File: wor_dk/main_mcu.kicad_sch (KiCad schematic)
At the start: 35 parts, among them IC201 TMUX1112PWR, IC202 TMUX1112PWR, J201 Prog_DUT, J202 Conn_02x04_Odd_Even, SW201 SW_Push, U201 nRF52840, Y201 32.768kHz, Y202 32MHz

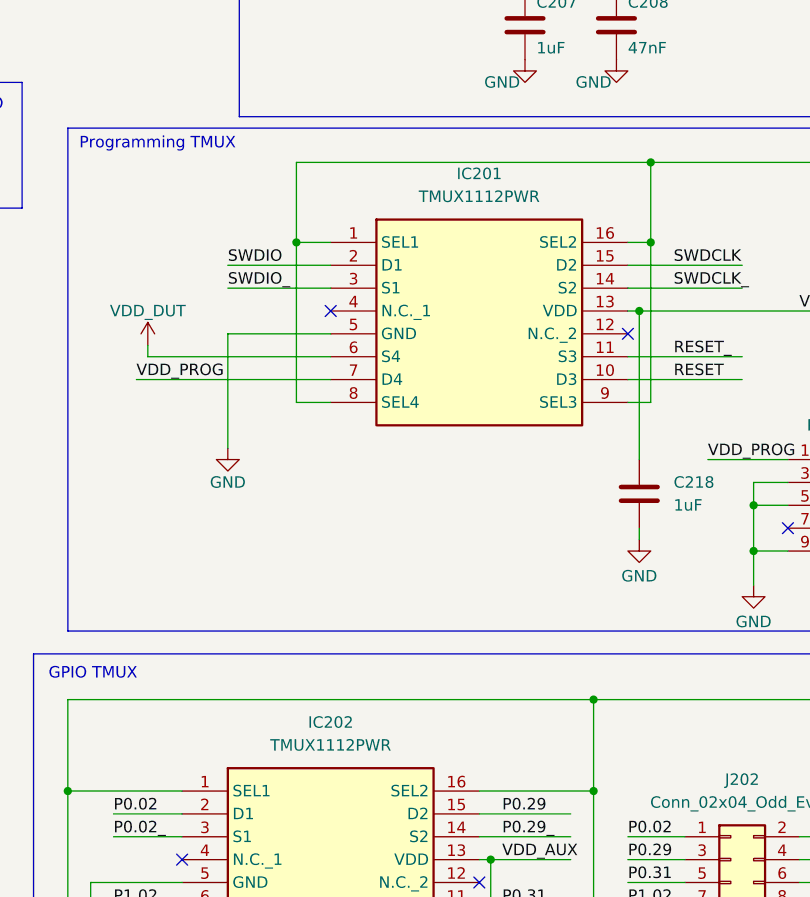
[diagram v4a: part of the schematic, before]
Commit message: wor_dk: library reorganization
- move everything to components
- use same directory naming as KiCAD installation
  (symbols/footprints/3dmodels)
- collect components into libraries rather than adding each file
  individually
- sanitize symbols according to our guidelines
  - sanitize symbol fields (e.g. Manufacturer Part Number -> MPN)
  - sanitize reference (IC -> U)
  - add ImportOrigin
  - add LCSC part number
  - remove unused fields
- link 3D models in footprints
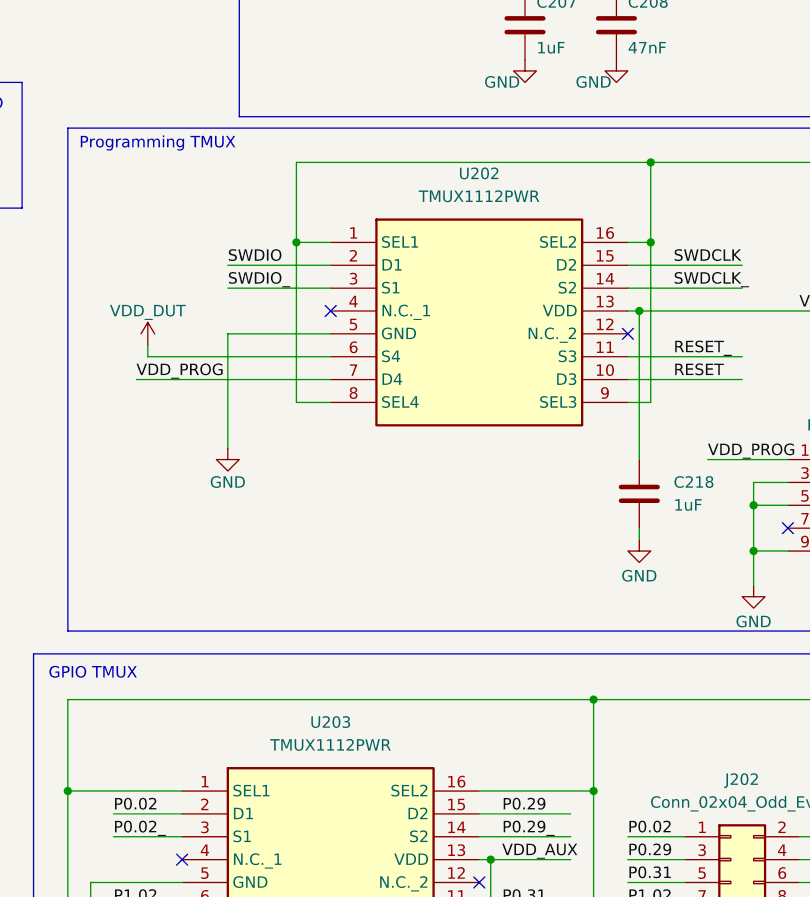
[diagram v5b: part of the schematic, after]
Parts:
- removed IC201, IC202: TMUX1112PWR, SOP65P640X120-16N, symbol TMUX1112PWR:TMUX1112PWR
- added U202, U203: TMUX1112PWR, TexasInstruments:SOP65P640X120-16N, symbol TexasInstruments:TMUX1112PWR
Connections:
- net GND: now also U202.5 (GND), U203.5 (GND)
- net GPIO_EN: now also U203.1 (SEL1), U203.16 (SEL2), U203.8 (SEL4), U203.9 (SEL3)
- net P0.02: now also U203.2 (D1)
- net P0.02_: now also U203.3 (S1)
- net P0.29: now also U203.15 (D2)
- net P0.29_: now also U203.14 (S2)
- net P0.31: now also U203.10 (D3)
- net P0.31_: now also U203.11 (S3)
- net P1.02: now also U203.7 (D4)
- net P1.02_: now also U203.6 (S4)
- net PROG_EN: now also U202.1 (SEL1), U202.16 (SEL2), U202.8 (SEL4), U202.9 (SEL3)
- net RESET: now also U202.10 (D3)
- net RESET_: now also U202.11 (S3)
- net SWDCLK: now also U202.15 (D2)
- net SWDCLK_: now also U202.14 (S2)
- net SWDIO: now also U202.2 (D1)
- net SWDIO_: now also U202.3 (S1)
- net VDD_AUX: now also U202.13 (VDD), U203.13 (VDD)
- net VDD_DUT: now also U202.6 (S4)
- net VDD_PROG: now also U202.7 (D4)

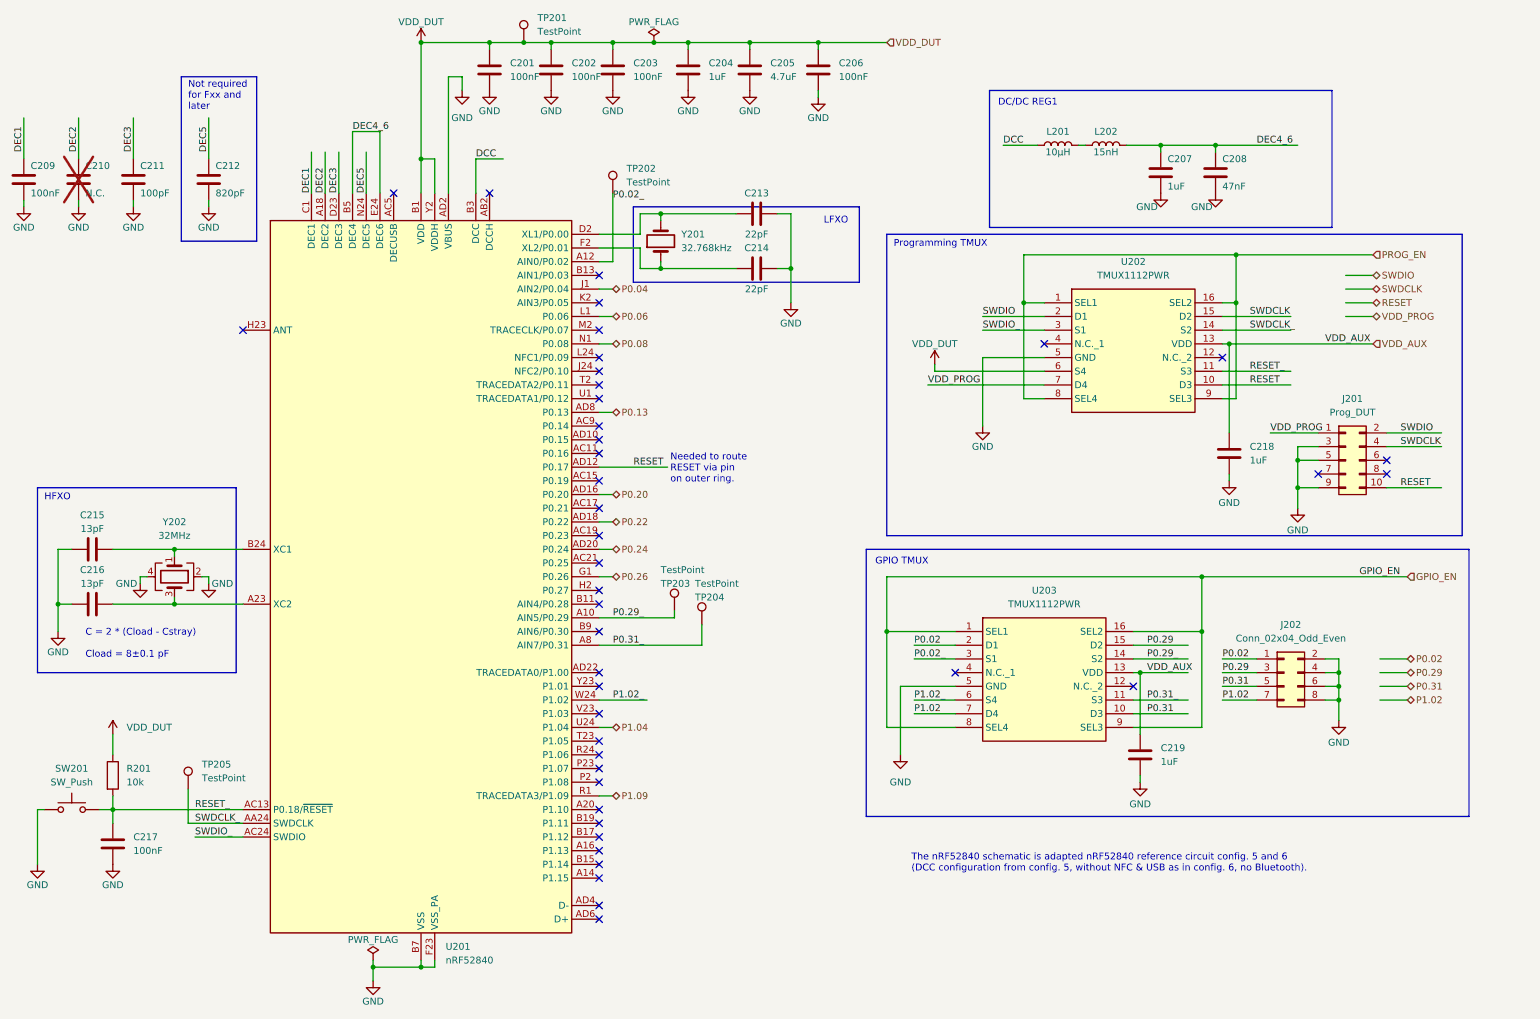
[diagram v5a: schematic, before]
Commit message: wor_dk: top-level connections & cleanup
- top-level connections for TMUX control & UART done (selection
  between FTDI and DAP Link via jumpers)
- all ERC errors & warnings cleaned up
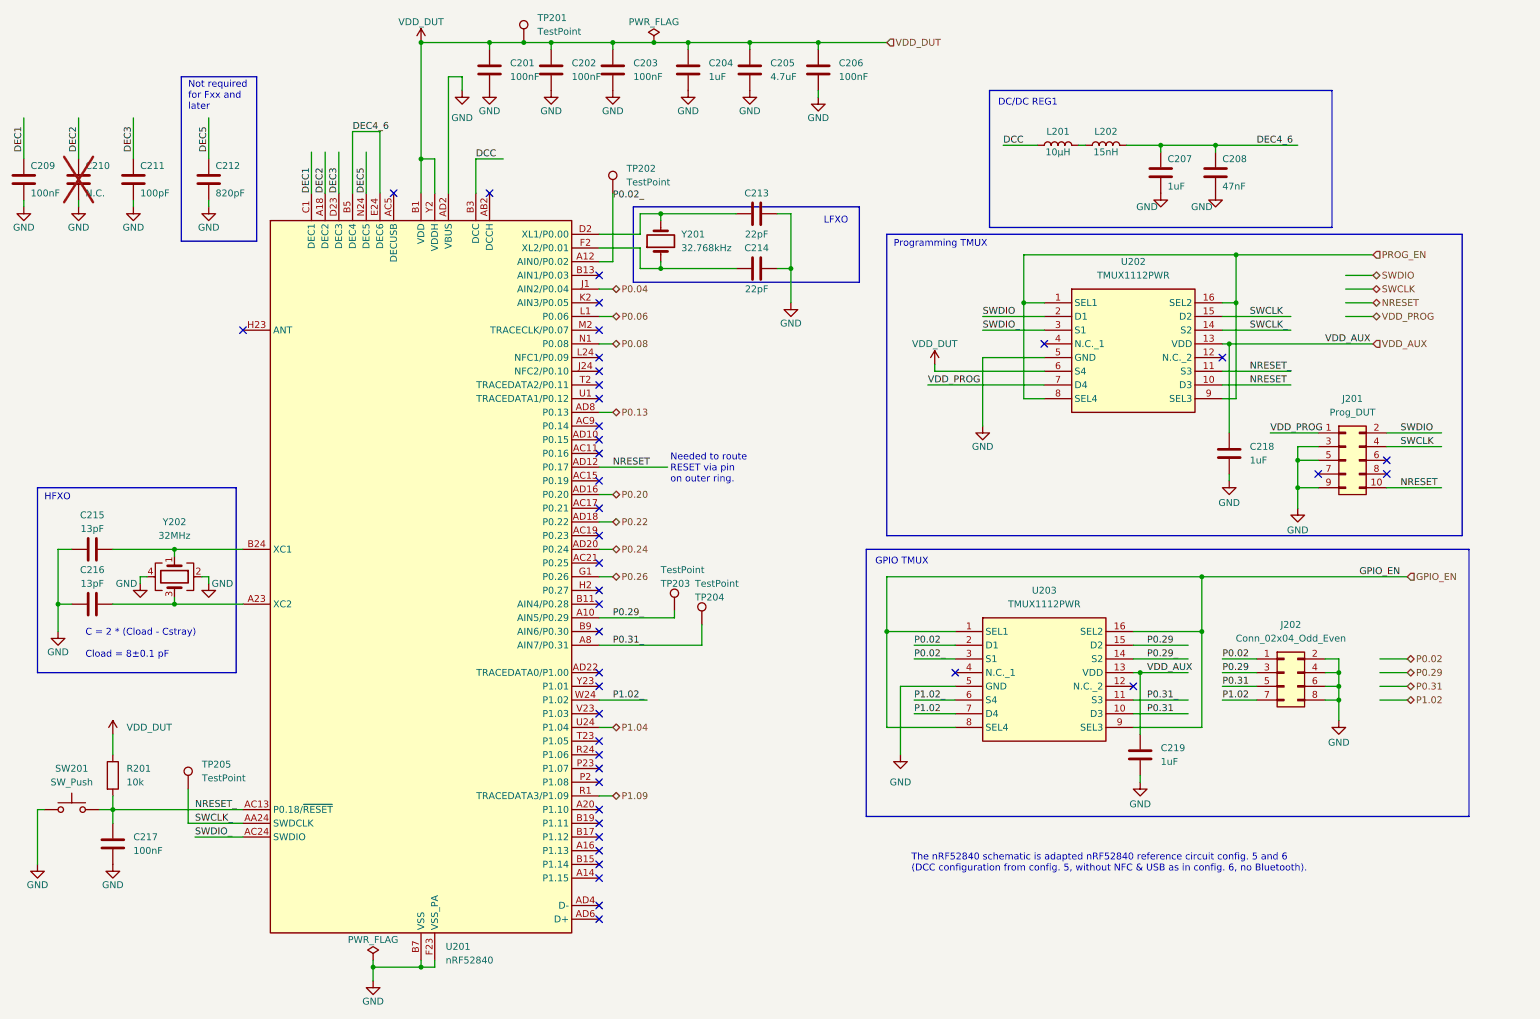
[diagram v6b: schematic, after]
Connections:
- net RESET renamed NRESET
- net RESET_ renamed NRESET_
- net SWDCLK renamed SWCLK
- net SWDCLK_ renamed SWCLK_
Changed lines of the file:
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@@
 		)
 	)
-	(label "SWDCLK"
+	(label "SWCLK"
 		(at 270.51 93.98 0)
 		(fields_autoplaced yes)
@@
 		)
 	)
-	(label "SWDCLK"
+	(label "SWCLK"
 		(at 242.57 69.85 0)
 		(fields_autoplaced yes)
@@
 		)
 	)
-	(label "RESET"
-		(at 128.27 97.79 0)
-		(fields_autoplaced yes)
-		(effects
-			(font
-				(size 1.27 1.27)
-			)
-			(justify left bottom)
-		)
-	)
-	(label "RESET"
+	(label "NRESET"
+		(at 124.46 97.79 0)
+		(fields_autoplaced yes)
+		(effects
+			(font
+				(size 1.27 1.27)
+			)
+			(justify left bottom)
+		)
+	)
+	(label "NRESET"
 		(at 242.57 82.55 0)
 		(fields_autoplaced yes)
@@
 		)
 	)
-	(label "RESET"
+	(label "NRESET"
 		(at 270.51 101.6 0)
 		(fields_autoplaced yes)
@@
 		)
 	)
-	(label "SWDCLK_"
+	(label "SWCLK_"
 		(at 242.57 72.39 0)
 		(fields_autoplaced yes)
@@
 		)
 	)
-	(label "RESET_"
+	(label "NRESET_"
 		(at 242.57 80.01 0)
 		(fields_autoplaced yes)
@@
 		)
 	)
-	(label "RESET_"
+	(label "NRESET_"
 		(at 46.99 161.29 0)
 		(fields_autoplaced yes)
@@
 		)
 	)
-	(label "SWDCLK_"
+	(label "SWCLK_"
 		(at 46.99 163.83 0)
 		(fields_autoplaced yes)
@@
 		)
 	)
-	(hierarchical_label "RESET"
+	(hierarchical_label "NRESET"
 		(shape tri_state)
 		(at 265.43 67.31 0)
@@
 		)
 	)
-	(hierarchical_label "SWDCLK"
+	(hierarchical_label "SWCLK"
 		(shape tri_state)
 		(at 265.43 64.77 0)

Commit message: wor_dk: cleanup & add test points & add pin headers
- test points are added for signals that only need to be measured to
  ensure proper functionality of the WoR DK
- pin headers are added for signals that may be useful during use of
  the WoR DK
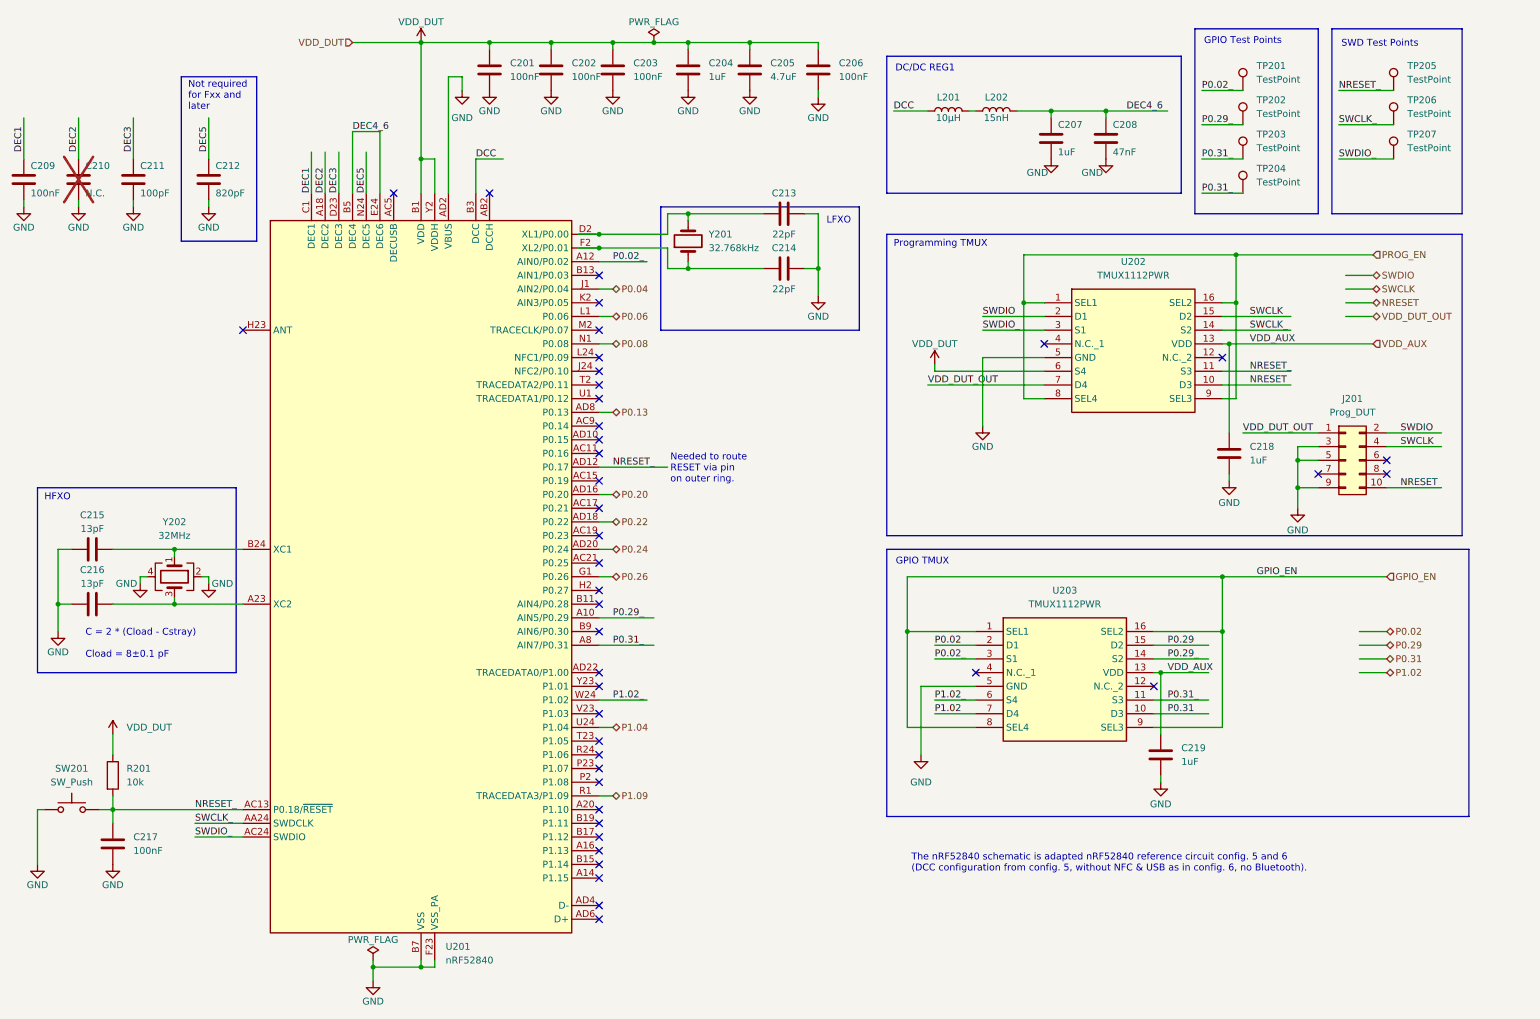
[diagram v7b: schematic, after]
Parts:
- removed J202: Conn_02x04_Odd_Even, symbol Connector_Generic:Conn_02x04_Odd_Even
- added TP206, TP207: TestPoint, symbol Connector:TestPoint
- TP201, TP202, TP203, TP204, TP205: footprint TestPoint:TestPoint_Pad_D1.0mm -> (none)
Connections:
- net NRESET: no longer U201.AD12 (P0.17)
- net NRESET_: now also TP205.1, U201.AD12 (P0.17)
- net P0.02_: now also TP201.1; no longer TP202.1
- net P0.29_: now also TP202.1; no longer TP203.1
- net P0.31_: now also TP203.1
- net SWCLK_: now also TP206.1; no longer TP205.1
- net SWDIO_: now also TP207.1
- net VDD_DUT: no longer TP201.1
- net VDD_PROG renamed VDD_DUT_OUT
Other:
- note added: "GPIO Test Points"
- note added: "SWD Test Points"
- moved on the sheet: C207, C208, C213, C214, C219, L201, L202, U203, Y201

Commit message: wor_dk: add footprints & part info for all resistors
All resistors are JLCPCB basic parts. Footprint 0402 is used for all
resistors, except for 0 Ω resistors, where 0805 is used.
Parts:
- R201: MPN (none) -> 0402WGF1002TCE
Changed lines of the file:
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@@
 			)
 		)
-		(property "Datasheet" "~"
+		(property "Datasheet" "https://wmsc.lcsc.com/wmsc/upload/file/pdf/v2/lcsc/2206010100_UNI-ROYAL-Uniroyal-Elec-0402WGF1002TCE_C25744.pdf"
 			(at 31.75 154.94 0)
 			(effects
@@
 			)
 		)
-		(property "Description" ""
+		(property "Description" "62.5mW Thick Film Resistors 50V ±100ppm/℃ ±1% 10kΩ 0402"
 			(at 31.75 154.94 0)
 			(effects
@@
 			(at 31.75 154.94 0)
 			(effects
+				(font
+					(size 1.27 1.27)
+				)
+				(hide yes)
+			)
+		)
+		(property "MPN" "0402WGF1002TCE"
+			(at 31.75 154.94 0)
+			(effects
